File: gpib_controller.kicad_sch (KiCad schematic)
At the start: 1 part

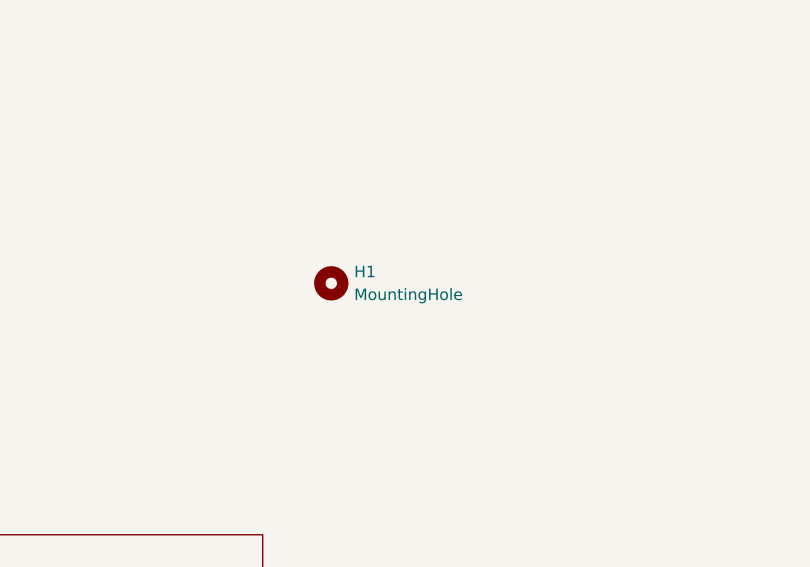
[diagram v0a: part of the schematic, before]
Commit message: Change board size, complete bottom routing, update (still broken) jobfile
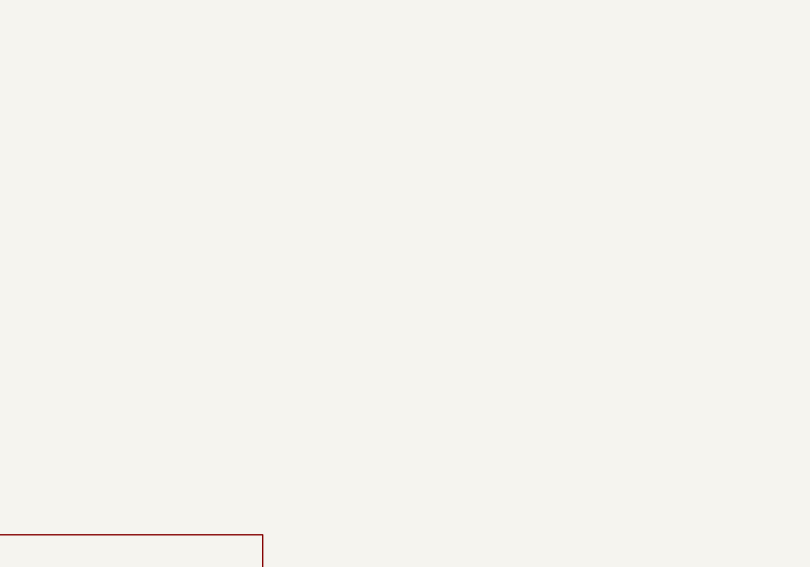
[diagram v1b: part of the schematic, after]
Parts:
- removed H1: MountingHole, MountingHole:MountingHole_2.1mm, symbol Mechanical:MountingHole
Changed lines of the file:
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@@
-		)
-	)
-	(symbol
-		(lib_id "Mechanical:MountingHole")
-		(at 109.22 200.66 0)
-		(unit 1)
-		(body_style 1)
-		(exclude_from_sim no)
-		(in_bom no)
-		(on_board yes)
-		(in_pos_files yes)
-		(dnp no)
-		(fields_autoplaced yes)
-		(property "Reference" "H1"
-			(at 111.76 199.39 0)
-			(show_name no)
-			(do_not_autoplace no)
-			(effects
-				(font
-					(size 1.27 1.27)
-				)
-				(justify left)
-			)
-		)
-		(property "Value" "MountingHole"
-			(at 111.76 201.93 0)
-			(show_name no)
-			(do_not_autoplace no)
-			(effects
-				(font
-					(size 1.27 1.27)
-				)
-				(justify left)
-			)
-		)
-		(property "Footprint" "MountingHole:MountingHole_2.1mm"
-			(at 109.22 200.66 0)
-			(hide yes)
-			(show_name no)
-			(do_not_autoplace no)
-			(effects
-				(font
-					(size 1.27 1.27)
-				)
-			)
-		)
-		(property "Datasheet" ""
-			(at 109.22 200.66 0)
-			(hide yes)
-			(show_name no)
-			(do_not_autoplace no)
-			(effects
-				(font
-					(size 1.27 1.27)
-				)
-			)
-		)
-		(property "Description" "Mounting Hole without connection"
-			(at 109.22 200.66 0)
-			(hide yes)
-			(show_name no)
-			(do_not_autoplace no)
-			(effects
-				(font
-					(size 1.27 1.27)
-				)
-			)
-		)
-		(instances
-			(project "gpib_controller"
-				(path "/0f352524-50ff-469d-9a68-783e183b0073"
-					(reference "H1")
-					(unit 1)
-				)
-			)
 		)
 	)

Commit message: Route GPIB pins
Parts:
- added H1: MountingHole, MountingHole:MountingHole_2.1mm, symbol Mechanical:MountingHole
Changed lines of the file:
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@@
+		)
+	)
+	(symbol
+		(lib_id "Mechanical:MountingHole")
+		(at 109.22 200.66 0)
+		(unit 1)
+		(body_style 1)
+		(exclude_from_sim no)
+		(in_bom no)
+		(on_board yes)
+		(in_pos_files yes)
+		(dnp no)
+		(fields_autoplaced yes)
+		(property "Reference" "H1"
+			(at 111.76 199.39 0)
+			(show_name no)
+			(do_not_autoplace no)
+			(effects
+				(font
+					(size 1.27 1.27)
+				)
+				(justify left)
+			)
+		)
+		(property "Value" "MountingHole"
+			(at 111.76 201.93 0)
+			(show_name no)
+			(do_not_autoplace no)
+			(effects
+				(font
+					(size 1.27 1.27)
+				)
+				(justify left)
+			)
+		)
+		(property "Footprint" "MountingHole:MountingHole_2.1mm"
+			(at 109.22 200.66 0)
+			(hide yes)
+			(show_name no)
+			(do_not_autoplace no)
+			(effects
+				(font
+					(size 1.27 1.27)
+				)
+			)
+		)
+		(property "Datasheet" ""
+			(at 109.22 200.66 0)
+			(hide yes)
+			(show_name no)
+			(do_not_autoplace no)
+			(effects
+				(font
+					(size 1.27 1.27)
+				)
+			)
+		)
+		(property "Description" "Mounting Hole without connection"
+			(at 109.22 200.66 0)
+			(hide yes)
+			(show_name no)
+			(do_not_autoplace no)
+			(effects
+				(font
+					(size 1.27 1.27)
+				)
+			)
+		)
+		(instances
+			(project "gpib_controller"
+				(path "/0f352524-50ff-469d-9a68-783e183b0073"
+					(reference "H1")
+					(unit 1)
+				)
+			)
 		)
 	)
